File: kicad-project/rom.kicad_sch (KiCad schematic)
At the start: 0 parts

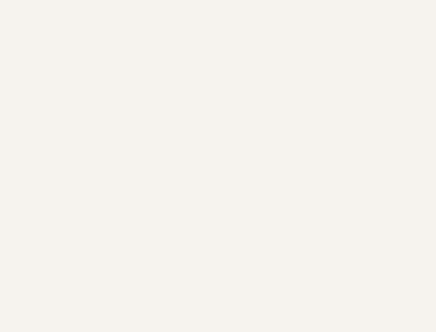
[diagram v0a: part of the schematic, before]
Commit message: Add kicad project and some initial schematics
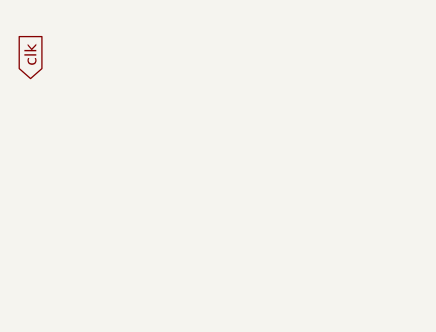
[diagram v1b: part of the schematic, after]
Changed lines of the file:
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@@
 (kicad_sch (version 20211123) (generator eeschema)
   (paper "A4")
+  (global_label "clk" (shape input) (at 88.9 63.5 90) (fields_autoplaced)
+    (effects (font (size 1.27 1.27)) (justify left))
+    (property "Intersheet References" "${INTERSHEET_REFS}" (id 0) (at 88.8206 58.305 90)
+      (effects (font (size 1.27 1.27)) (justify left))
+    )
+  )
   (hierarchical_label "Address" (shape input) (at 241.3 101.6 0)
     (effects (font (size 1.27 1.27)) (justify left))

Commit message: address register and more
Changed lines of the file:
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@@
     (effects (font (size 1.27 1.27)) (justify right))
+  )
+  (hierarchical_label "Address" (shape input) (at 158.75 63.5 90)
+    (effects (font (size 1.27 1.27)) (justify left))
   )
   (hierarchical_label "Operand" (shape output) (at 152.4 152.4 270)
